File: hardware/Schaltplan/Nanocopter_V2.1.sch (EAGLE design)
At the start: 123 parts, among them IC1 CY7C68013A-56QFNLFXC, M1A TPSQTP20SQ, M1B TPSQTP20SQ, M1C TPSQTP20SQ, M2A TPSQTP20SQ, M2B TPSQTP20SQ, M2C TPSQTP20SQ, M3A TPSQTP20SQ, M3B TPSQTP20SQ, M3C TPSQTP20SQ, M4A TPSQTP20SQ, M4B TPSQTP20SQ, M4C TPSQTP20SQ, T5 IRLML2502, T6 IRLML2502, T7 IRLML2502, T8 IRLML2502, U2 PRTR5V0U2X, U3 LM3480-3.3, X1 USBSMD, X2 53261-08, X3 53261-06, X4 53261-03, X5 53261-03, X6 53261-06

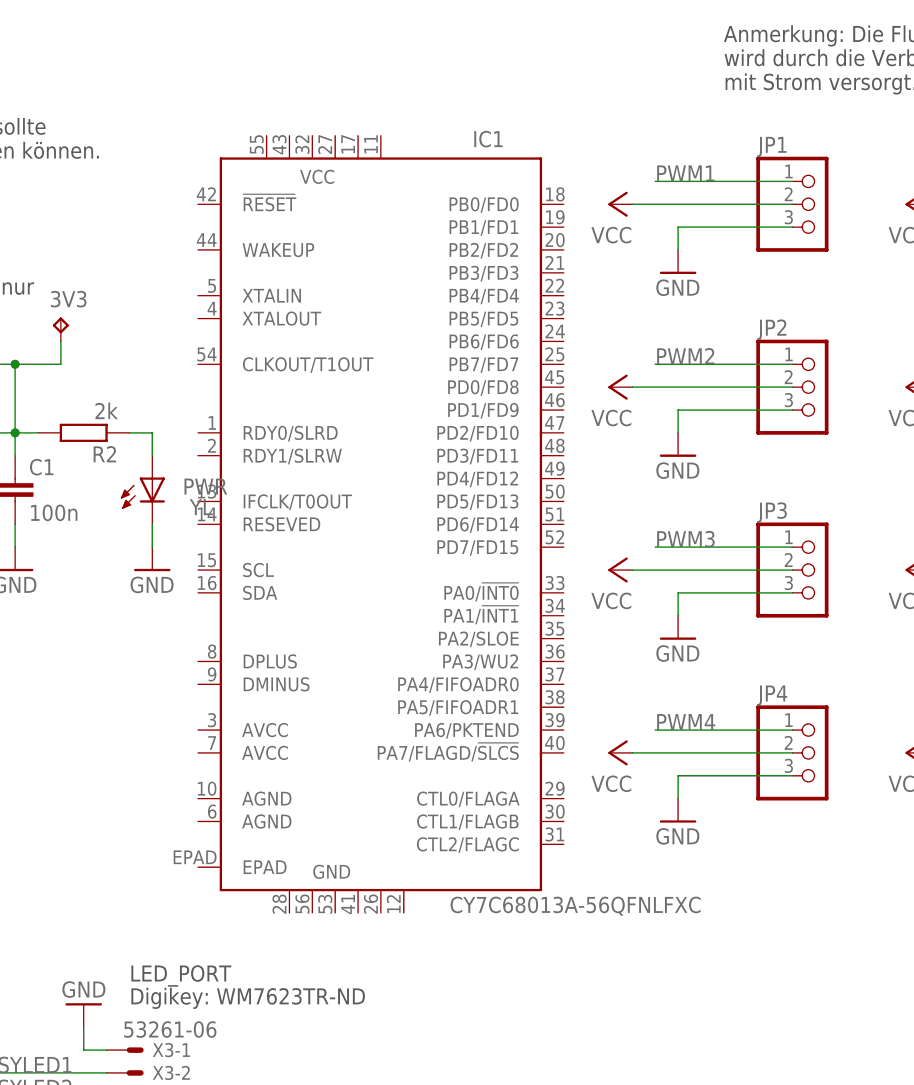
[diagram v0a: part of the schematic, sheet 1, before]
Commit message: Dimensionen von SimpleControl aktualisiert
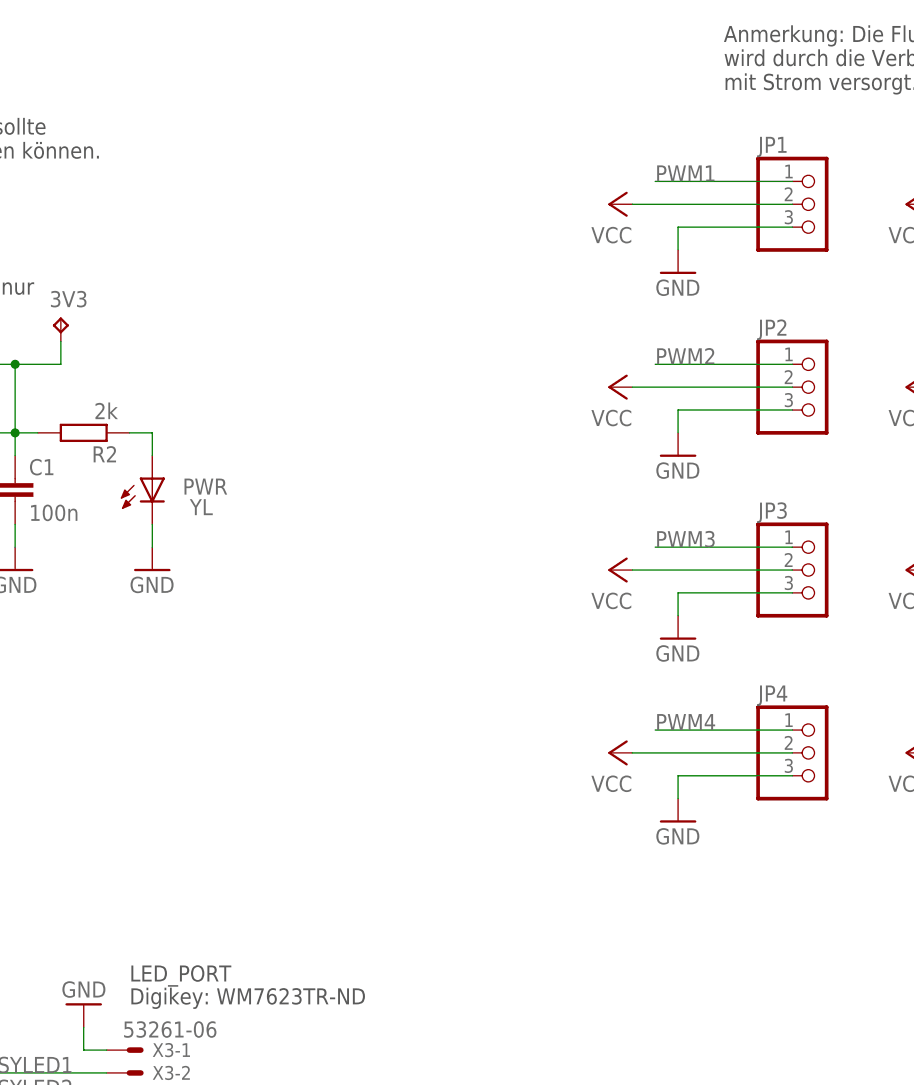
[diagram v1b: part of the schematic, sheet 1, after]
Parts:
- removed IC1: CY7C68013A-56QFNLFXC, cypress:CY7C68013A-56QFNLFXC
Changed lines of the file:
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@@
 <part name="SJ3" library="jumper" deviceset="SJ2W" device=""/>
 <part name="U$6" library="irf" deviceset="IRF7321" device=""/>
-<part name="IC1" library="cypress" deviceset="CY7C6801*A-56QFN" device="LFXC" technology="3"/>
 </parts>
 <sheets>
@@
 <instance part="JP10" gate="G$1" x="162.56" y="198.12" rot="R180"/>
 <instance part="SJ2" gate="1" x="200.66" y="208.28" rot="R90"/>
-<instance part="IC1" gate="G$1" x="276.86" y="187.96"/>
 </instances>
 <busses>
